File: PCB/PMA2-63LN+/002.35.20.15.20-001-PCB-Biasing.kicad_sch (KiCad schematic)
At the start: 9 parts

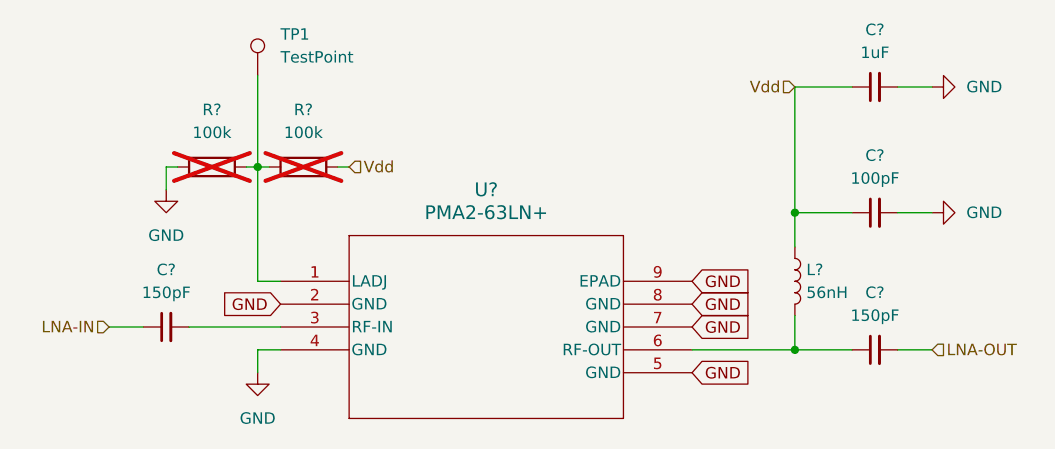
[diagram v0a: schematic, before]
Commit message: pcb: added boms, updated readmes, changed silkscreen from dfs/ems to nmsm
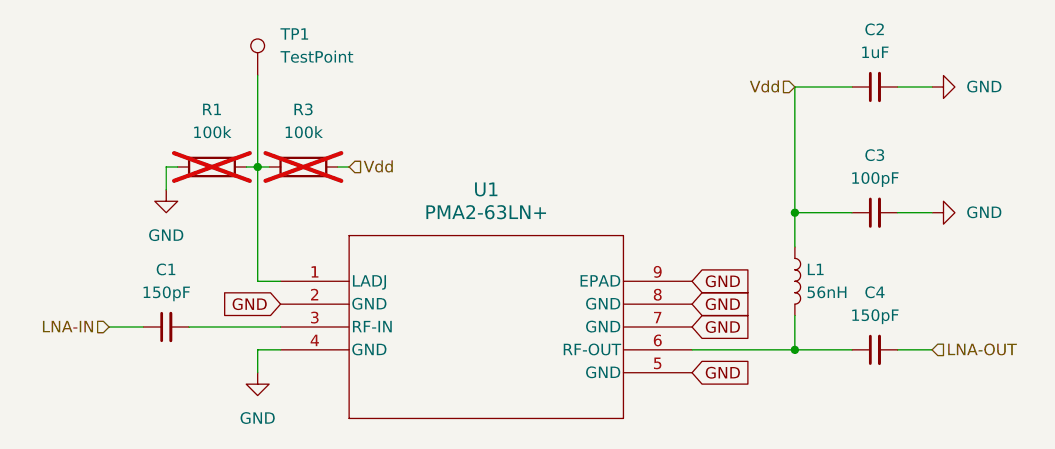
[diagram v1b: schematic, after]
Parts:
- C1, C2, C3, C4: renamed from C?; Link (none) -> https://www.digikey.com/en/products/detail/murata-electroni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
- L1: renamed from L?; Link (none) -> https://www.mouser.com/ProductDetail/Coilcraft/0402CS-56NXG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
- U1: renamed from U?; Link (none) -> https://www.minicircuits.com/WebStore/dashboard.html?model=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
- gave numbers to parts that had none: 2
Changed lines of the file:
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@@
   (symbol (lib_id "power:GND") (at 196.85 97.79 90) (unit 1)
     (in_bom yes) (on_board yes) (dnp no) (fields_autoplaced)
-    (property "Reference" "#PWR?" (at 203.2 97.79 0)
+    (property "Reference" "#PWR016" (at 203.2 97.79 0)
       (effects (font (size 1.27 1.27)) hide)
     )
@@
     (instances
       (project "002.35.20.15.20-001-PCB-LNA"
-        (path "/a33db424-96f2-4015-ba95-8b9f2330ef17"
-          (reference "#PWR?") (unit 1)
-        )
         (path "/a33db424-96f2-4015-ba95-8b9f2330ef17/9ff85c99-1040-4eb9-b5d8-3cc01caa0e77"
           (reference "#PWR016") (unit 1)
@@
   (symbol (lib_id "rf-dfs:C_Small") (at 190.5 83.82 90) (unit 1)
     (in_bom yes) (on_board yes) (dnp no) (fields_autoplaced)
-    (property "Reference" "C?" (at 190.5063 77.47 90)
+    (property "Reference" "C2" (at 190.5063 77.47 90)
       (effects (font (size 1.27 1.27)))
     )
@@
       (effects (font (size 1.27 1.27)) hide)
     )
-    (pin "1")
-    (pin "2")
-    (instances
-      (project "002.35.20.15.20-001-PCB-LNA"
-        (path "/a33db424-96f2-4015-ba95-8b9f2330ef17"
-          (reference "C?") (unit 1)
-        )
+    (property "Link" "https://www.digikey.com/en/products/detail/murata-electronics/GRM155R61E105KA12D/4905139" (at 190.5 83.82 0)
+      (effects (font (size 1.27 1.27)) hide)
+    )
+    (pin "1")
+    (pin "2")
+    (instances
+      (project "002.35.20.15.20-001-PCB-LNA"
         (path "/a33db424-96f2-4015-ba95-8b9f2330ef17/9ff85c99-1040-4eb9-b5d8-3cc01caa0e77"
           (reference "C2") (unit 1)
@@
   (symbol (lib_id "rf-dfs:L") (at 181.61 105.41 0) (unit 1)
     (in_bom yes) (on_board yes) (dnp no) (fields_autoplaced)
-    (property "Reference" "L?" (at 182.88 104.14 0)
+    (property "Reference" "L1" (at 182.88 104.14 0)
       (effects (font (size 1.27 1.27)) (justify left))
     )
@@
       (effects (font (size 1.27 1.27)) hide)
     )
-    (pin "1")
-    (pin "2")
-    (instances
-      (project "002.35.20.15.20-001-PCB-LNA"
-        (path "/a33db424-96f2-4015-ba95-8b9f2330ef17"
-          (reference "L?") (unit 1)
-        )
+    (property "Link" "https://www.mouser.com/ProductDetail/Coilcraft/0402CS-56NXGLW?qs=JVZp5BaCFzgAnjagIlSj3A%3D%3D" (at 181.61 105.41 0)
+      (effects (font (size 1.27 1.27)) hide)
+    )
+    (pin "1")
+    (pin "2")
+    (instances
+      (project "002.35.20.15.20-001-PCB-LNA"
         (path "/a33db424-96f2-4015-ba95-8b9f2330ef17/9ff85c99-1040-4eb9-b5d8-3cc01caa0e77"
           (reference "L1") (unit 1)
@@
   (symbol (lib_id "rf-dfs:C_Small") (at 190.5 97.79 90) (unit 1)
     (in_bom yes) (on_board yes) (dnp no) (fields_autoplaced)
-    (property "Reference" "C?" (at 190.5063 91.44 90)
+    (property "Reference" "C3" (at 190.5063 91.44 90)
       (effects (font (size 1.27 1.27)))
     )
@@
       (effects (font (size 1.27 1.27)) hide)
     )
-    (pin "1")
-    (pin "2")
-    (instances
-      (project "002.35.20.15.20-001-PCB-LNA"
-        (path "/a33db424-96f2-4015-ba95-8b9f2330ef17"
-          (reference "C?") (unit 1)
-        )
+    (property "Link" "https://www.digikey.com/en/products/detail/murata-electronics/GRM1555C1H101JA01D/3693829" (at 190.5 97.79 0)
+      (effects (font (size 1.27 1.27)) hide)
+    )
+    (pin "1")
+    (pin "2")
+    (instances
+      (project "002.35.20.15.20-001-PCB-LNA"
         (path "/a33db424-96f2-4015-ba95-8b9f2330ef17/9ff85c99-1040-4eb9-b5d8-3cc01caa0e77"
           (reference "C3") (unit 1)
@@
   (symbol (lib_name "PMA2-63LN+_1") (lib_id "rf-dfs:PMA2-63LN+_1") (at 124.46 105.41 0) (unit 1)
     (in_bom yes) (on_board yes) (dnp no) (fields_autoplaced)
-    (property "Reference" "U?" (at 147.32 95.25 0)
+    (property "Reference" "U1" (at 147.32 95.25 0)
       (effects (font (size 1.524 1.524)))
     )
@@
     (property "Datasheet" "PMA2-63LN+" (at 124.46 105.41 0)
       (effects (font (size 1.27 1.27) italic) hide)
+    )
+    (property "Link" "https://www.minicircuits.com/WebStore/dashboard.html?model=PMA2-63LN%2B" (at 124.46 105.41 0)
+      (effects (font (size 1.27 1.27)) hide)
     )
     (pin "1")
@@
     (instances
       (project "002.35.20.15.20-001-PCB-LNA"
-        (path "/a33db424-96f2-4015-ba95-8b9f2330ef17"
-          (reference "U?") (unit 1)
-        )
         (path "/a33db424-96f2-4015-ba95-8b9f2330ef17/9ff85c99-1040-4eb9-b5d8-3cc01caa0e77"
           (reference "U1") (unit 1)
@@
   (symbol (lib_id "rf-dfs:C_Small") (at 190.5 113.03 90) (unit 1)
     (in_bom yes) (on_board yes) (dnp no) (fields_autoplaced)
-    (property "Reference" "C?" (at 190.5063 106.68 90)
+    (property "Reference" "C4" (at 190.5063 106.68 90)
       (effects (font (size 1.27 1.27)))
     )
@@
       (effects (font (size 1.27 1.27)) hide)
     )
-    (pin "1")
-    (pin "2")
-    (instances
-      (project "002.35.20.15.20-001-PCB-LNA"
-        (path "/a33db424-96f2-4015-ba95-8b9f2330ef17"
-          (reference "C?") (unit 1)
-        )
+    (property "Link" "https://www.digikey.com/en/products/detail/murata-electronics/GRM1555C1H151JA01J/2543888" (at 190.5 113.03 0)
+      (effects (font (size 1.27 1.27)) hide)
+    )
+    (pin "1")
+    (pin "2")
+    (instances
+      (project "002.35.20.15.20-001-PCB-LNA"
         (path "/a33db424-96f2-4015-ba95-8b9f2330ef17/9ff85c99-1040-4eb9-b5d8-3cc01caa0e77"
           (reference "C4") (unit 1)
@@
   (symbol (lib_id "power:GND") (at 111.76 95.25 0) (unit 1)
     (in_bom yes) (on_board yes) (dnp no) (fields_autoplaced)
-    (property "Reference" "#PWR?" (at 111.76 101.6 0)
+    (property "Reference" "#PWR01" (at 111.76 101.6 0)
       (effects (font (size 1.27 1.27)) hide)
     )
@@
     (instances
       (project "002.35.20.15.20-001-PCB-LNA"
-        (path "/a33db424-96f2-4015-ba95-8b9f2330ef17"
-          (reference "#PWR?") (unit 1)
-        )
         (path "/a33db424-96f2-4015-ba95-8b9f2330ef17/9ff85c99-1040-4eb9-b5d8-3cc01caa0e77"
           (reference "#PWR01") (unit 1)
@@
   (symbol (lib_id "rf-dfs:C_Small") (at 111.76 110.49 90) (unit 1)
     (in_bom yes) (on_board yes) (dnp no) (fields_autoplaced)
-    (property "Reference" "C?" (at 111.7663 104.14 90)
+    (property "Reference" "C1" (at 111.7663 104.14 90)
       (effects (font (size 1.27 1.27)))
     )
@@
       (effects (font (size 1.27 1.27)) hide)
     )
-    (pin "1")
-    (pin "2")
-    (instances
-      (project "002.35.20.15.20-001-PCB-LNA"
-        (path "/a33db424-96f2-4015-ba95-8b9f2330ef17"
-          (reference "C?") (unit 1)
-        )
+    (property "Link" "https://www.digikey.com/en/products/detail/murata-electronics/GRM1555C1H151JA01J/2543888" (at 111.76 110.49 0)
+      (effects (font (size 1.27 1.27)) hide)
+    )
+    (pin "1")
+    (pin "2")
+    (instances
+      (project "002.35.20.15.20-001-PCB-LNA"
         (path "/a33db424-96f2-4015-ba95-8b9f2330ef17/9ff85c99-1040-4eb9-b5d8-3cc01caa0e77"
           (reference "C1") (unit 1)
@@
       (effects (font (size 1.27 1.27)) hide)
     )
+    (property "Link" "" (at 121.92 82.55 0)
+      (effects (font (size 1.27 1.27)) hide)
+    )
     (pin "1")
     (instances
@@
   (symbol (lib_id "rf-dfs:R") (at 116.84 92.71 90) (unit 1)
     (in_bom yes) (on_board yes) (dnp yes) (fields_autoplaced)
-    (property "Reference" "R?" (at 116.84 86.36 90)
+    (property "Reference" "R1" (at 116.84 86.36 90)
       (effects (font (size 1.27 1.27)))
     )
@@
       (effects (font (size 1.27 1.27)) hide)
     )
-    (pin "1")
-    (pin "2")
-    (instances
-      (project "002.35.20.15.20-001-PCB-LNA"
-        (path "/a33db424-96f2-4015-ba95-8b9f2330ef17"
-          (reference "R?") (unit 1)
-        )
+    (property "Link" "" (at 116.84 92.71 0)
+      (effects (font (size 1.27 1.27)) hide)
+    )
+    (pin "1")
+    (pin "2")
+    (instances
+      (project "002.35.20.15.20-001-PCB-LNA"
         (path "/a33db424-96f2-4015-ba95-8b9f2330ef17/9ff85c99-1040-4eb9-b5d8-3cc01caa0e77"
           (reference "R1") (unit 1)
@@
   (symbol (lib_id "power:GND") (at 196.85 83.82 90) (unit 1)
     (in_bom yes) (on_board yes) (dnp no) (fields_autoplaced)
-    (property "Reference" "#PWR?" (at 203.2 83.82 0)
+    (property "Reference" "#PWR06" (at 203.2 83.82 0)
       (effects (font (size 1.27 1.27)) hide)
     )
@@
     (instances
       (project "002.35.20.15.20-001-PCB-LNA"
-        (path "/a33db424-96f2-4015-ba95-8b9f2330ef17"
-          (reference "#PWR?") (unit 1)
-        )
         (path "/a33db424-96f2-4015-ba95-8b9f2330ef17/9ff85c99-1040-4eb9-b5d8-3cc01caa0e77"
           (reference "#PWR06") (unit 1)
@@
   (symbol (lib_id "power:GND") (at 121.92 115.57 0) (unit 1)
     (in_bom yes) (on_board yes) (dnp no) (fields_autoplaced)
-    (property "Reference" "#PWR?" (at 121.92 121.92 0)
+    (property "Reference" "#PWR05" (at 121.92 121.92 0)
       (effects (font (size 1.27 1.27)) hide)
     )
@@
     (instances
       (project "002.35.20.15.20-001-PCB-LNA"
-        (path "/a33db424-96f2-4015-ba95-8b9f2330ef17"
-          (reference "#PWR?") (unit 1)
-        )
         (path "/a33db424-96f2-4015-ba95-8b9f2330ef17/9ff85c99-1040-4eb9-b5d8-3cc01caa0e77"
           (reference "#PWR05") (unit 1)
@@
   (symbol (lib_id "rf-dfs:R") (at 127 92.71 90) (unit 1)
     (in_bom yes) (on_board yes) (dnp yes) (fields_autoplaced)
-    (property "Reference" "R?" (at 127 86.36 90)
+    (property "Reference" "R3" (at 127 86.36 90)
       (effects (font (size 1.27 1.27)))
     )
@@
       (effects (font (size 1.27 1.27)) hide)
     )
-    (pin "1")
-    (pin "2")
-    (instances
-      (project "002.35.20.15.20-001-PCB-LNA"
-        (path "/a33db424-96f2-4015-ba95-8b9f2330ef17"
-          (reference "R?") (unit 1)
-        )
+    (property "Link" "" (at 127 92.71 0)
+      (effects (font (size 1.27 1.27)) hide)
+    )
+    (pin "1")
+    (pin "2")
+    (instances
+      (project "002.35.20.15.20-001-PCB-LNA"
         (path "/a33db424-96f2-4015-ba95-8b9f2330ef17/9ff85c99-1040-4eb9-b5d8-3cc01caa0e77"
           (reference "R3") (unit 1)
